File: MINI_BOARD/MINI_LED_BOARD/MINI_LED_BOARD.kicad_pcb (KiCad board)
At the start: 2 copper layers, 35 parts, among them J1 Conn_ARM_SWD_TagConnect_TC2030, J2 430450428, U1 MSPM0C1103SDDFR, U4 TPS76333DBVR

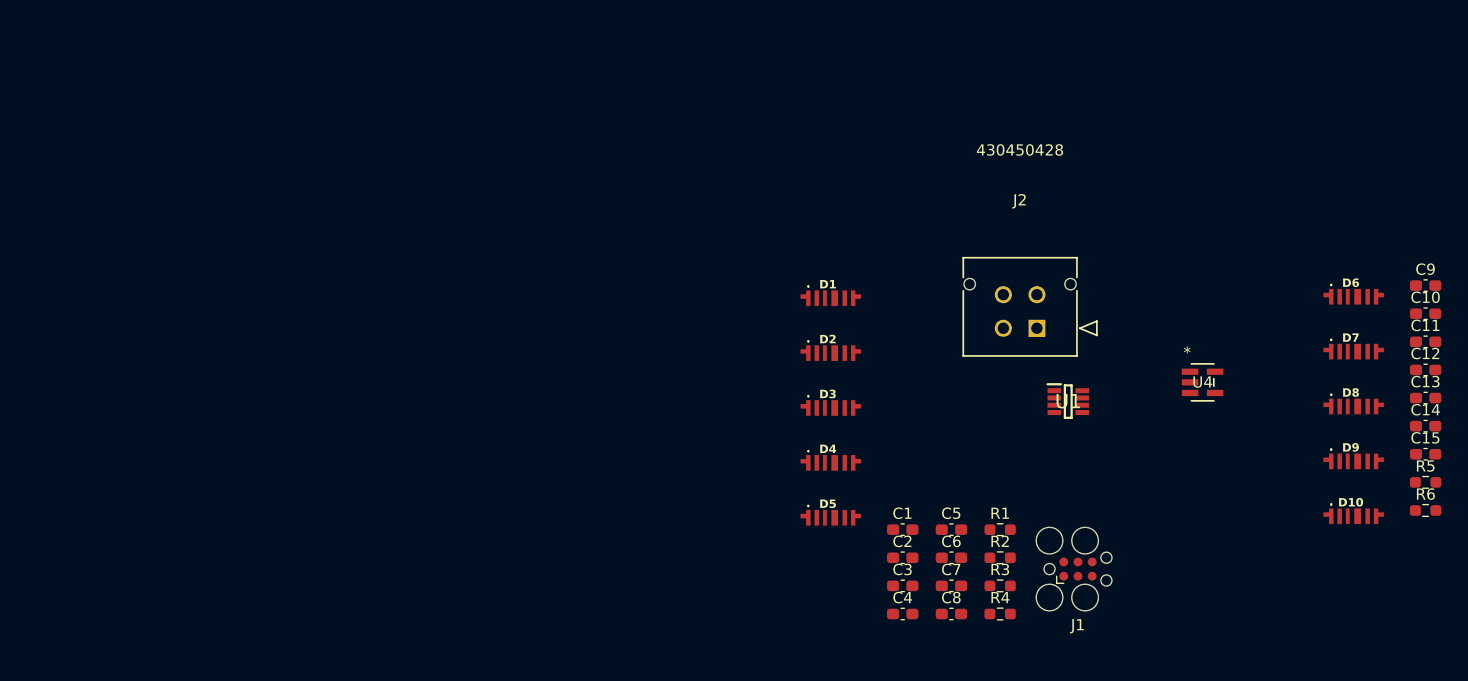
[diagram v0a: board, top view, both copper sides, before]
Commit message: Start laying out components
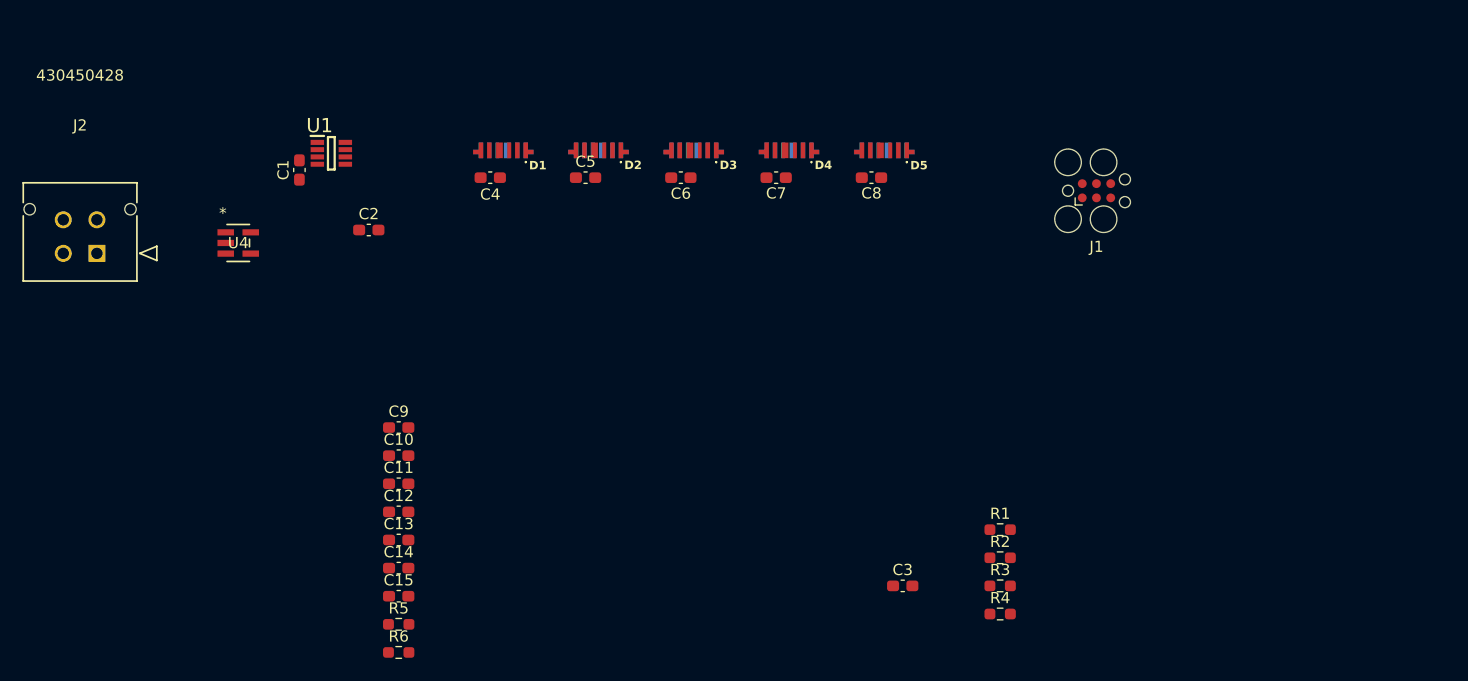
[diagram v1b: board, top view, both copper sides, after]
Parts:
- D10, D6, D7, D8, D9: moved to B.Cu
- moved C10 92.6 mm to (73.3, 82.5)
- moved C11 92.6 mm to (73.3, 85.0)
- moved C12 92.6 mm to (73.3, 87.5)
- moved C13 92.6 mm to (73.3, 90.0)
- moved C14 92.6 mm to (73.3, 92.5)
- moved C15 92.6 mm to (73.3, 95.1)
- moved C9 92.6 mm to (73.3, 80.0)
- moved R5 92.6 mm to (73.3, 97.6)
- moved R6 92.6 mm to (73.3, 100.1)
- moved U4 87.0 mm to (59.0, 63.5)
- moved J2 84.2 mm to (46.3, 64.4)
- moved D6 77.1 mm to (82.6, 54.9)
- moved D7 69.9 mm to (91.1, 54.9)
- moved U1 69.4 mm to (67.3, 55.5)
- moved D8 63.4 mm to (99.6, 54.9)
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
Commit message: Complete more major layout placement
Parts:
- C10, C11, C12, C13, C9: moved to B.Cu
- moved R1 66.2 mm to (70.6, 54.5)
- moved J1 63.0 mm to (73.0, 66.8)
- moved R3 62.4 mm to (78.2, 55.3), turned to 90 degrees
- moved C3 61.1 mm to (70.6, 55.9), turned to 180 degrees
- moved R2 59.5 mm to (78.1, 57.7), turned to 180 degrees
- moved C13 55.1 mm to (117.9, 57.7), turned to 180 degrees
- moved C12 46.8 mm to (109.4, 57.7), turned to 180 degrees
- moved R6 43.6 mm to (65.9, 57.1), turned to 180 degrees
- moved C15 40.1 mm to (65.9, 55.7)
- moved R5 39.7 mm to (65.9, 58.6)
- moved C14 39.2 mm to (59.7, 55.7), turned to -90 degrees
- moved C11 38.8 mm to (100.8, 57.7), turned to 180 degrees
- moved R4 36.8 mm to (123.6, 60.0)
- moved C10 31.3 mm to (92.3, 57.7), turned to 180 degrees
- moved C9 24.7 mm to (83.8, 57.7), turned to 180 degrees
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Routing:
- net Net-(U4-NC/FB): track 0.00 -> 4.41 mm
- net GND: track 0.00 -> 3.64 mm
- net +3.3V: track 0.00 -> 3.09 mm
- net +5V: track 0.00 -> 1.81 mm

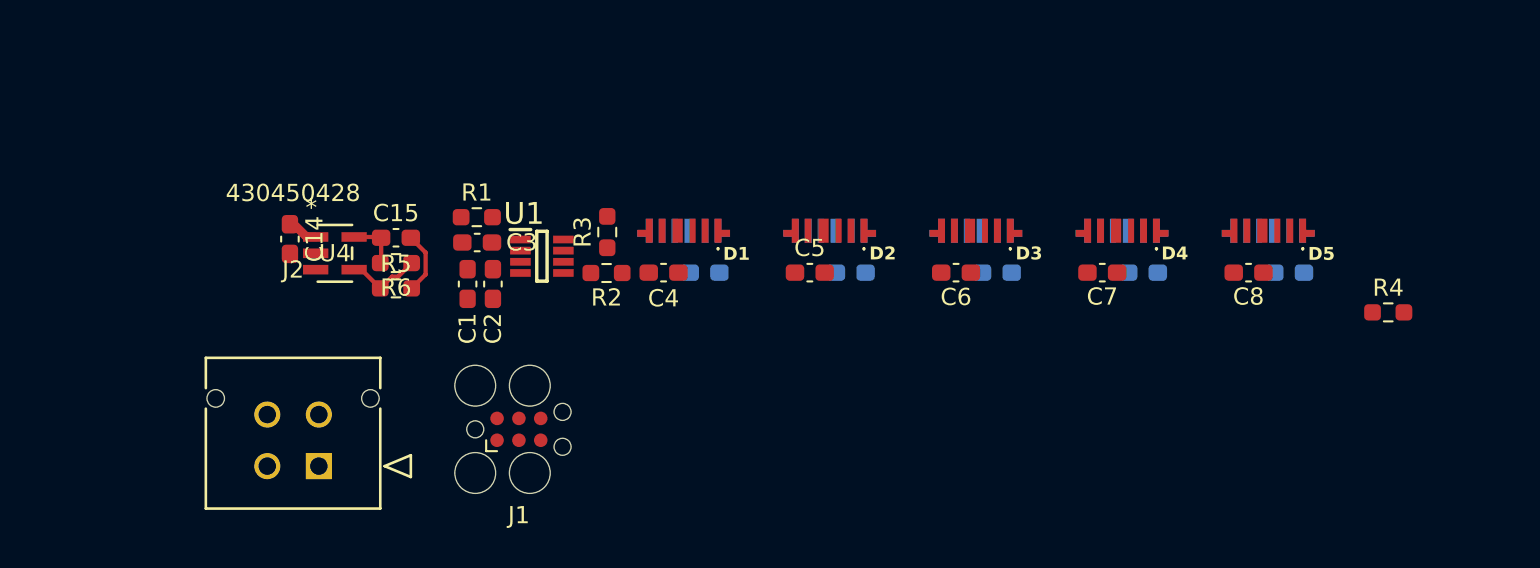
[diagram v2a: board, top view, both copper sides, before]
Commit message: Add more footprints and adjust layout placements
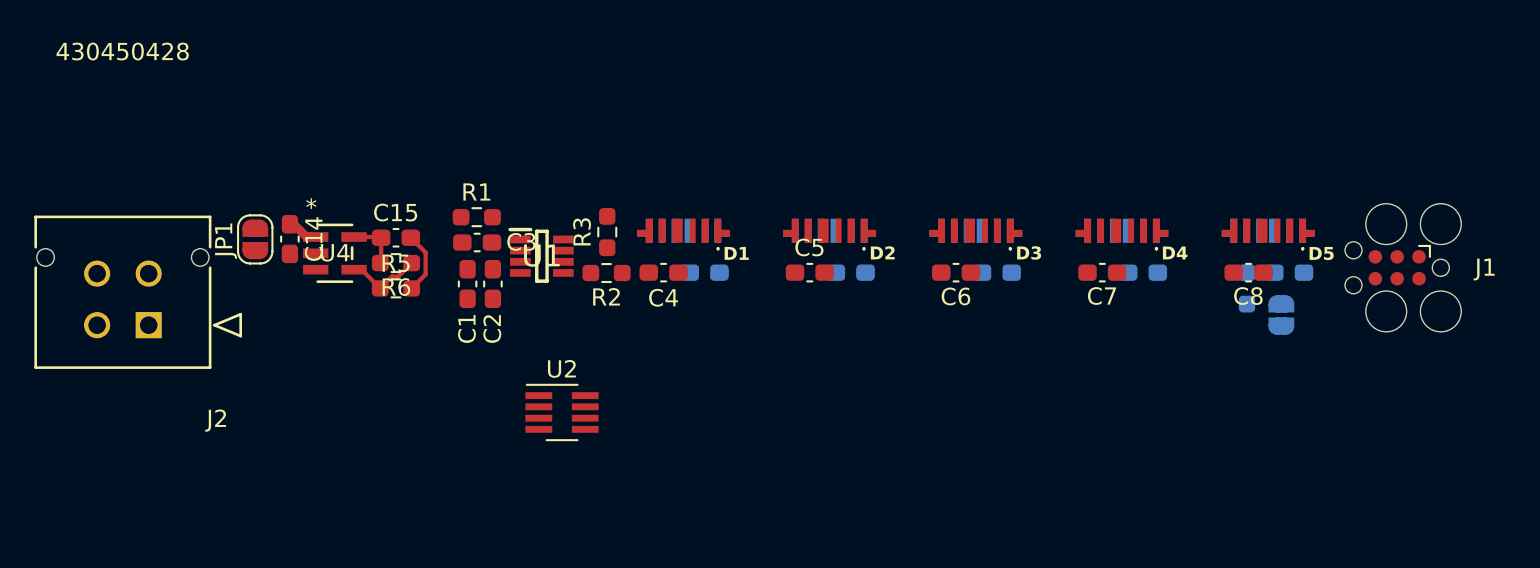
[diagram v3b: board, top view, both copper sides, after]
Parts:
- added JP1: SolderJumper_2_Open, Jumper:SolderJumper-2_P1.3mm_Open_RoundedPad1.0x1.5mm, F.Cu at (57.7, 55.7)
- added JP2: SolderJumper_2_Open, Jumper:SolderJumper-2_P1.3mm_Open_RoundedPad1.0x1.5mm, B.Cu at (117.4, 60.2)
- added U2: TCAN334, Package_TO_SOT_SMD:SOT-23-8_Handsoldering, F.Cu at (75.5, 65.8)
- R4: moved to B.Cu
- moved J1 52.0 mm to (124.1, 57.4), turned to 180 degrees
- moved J2 12.9 mm to (51.5, 60.7)
- moved R4 8.34 mm to (115.4, 58.6), turned to -90 degrees
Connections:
- R4 pad 2: unconnected-(R4-Pad2) -> Net-(JP2-A)

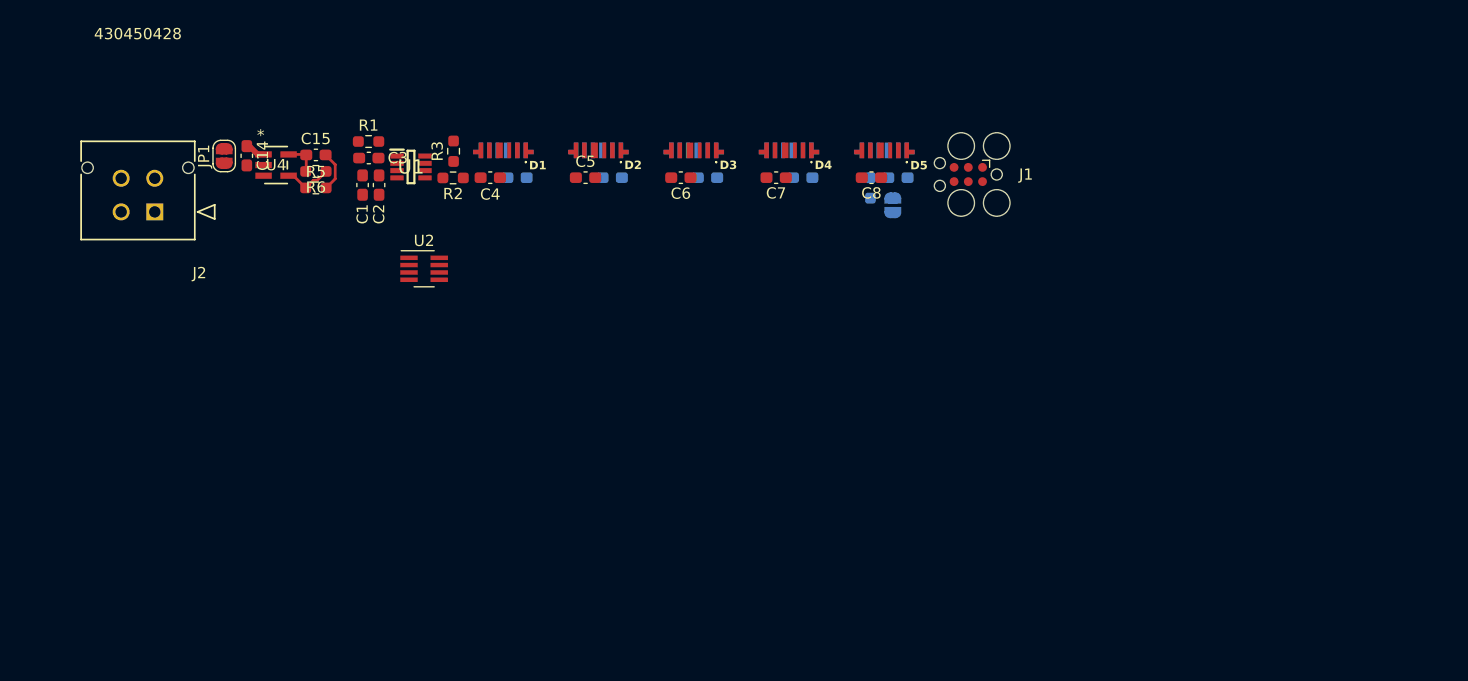
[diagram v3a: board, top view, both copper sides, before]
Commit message: Add more TCAN passives and mess with layout
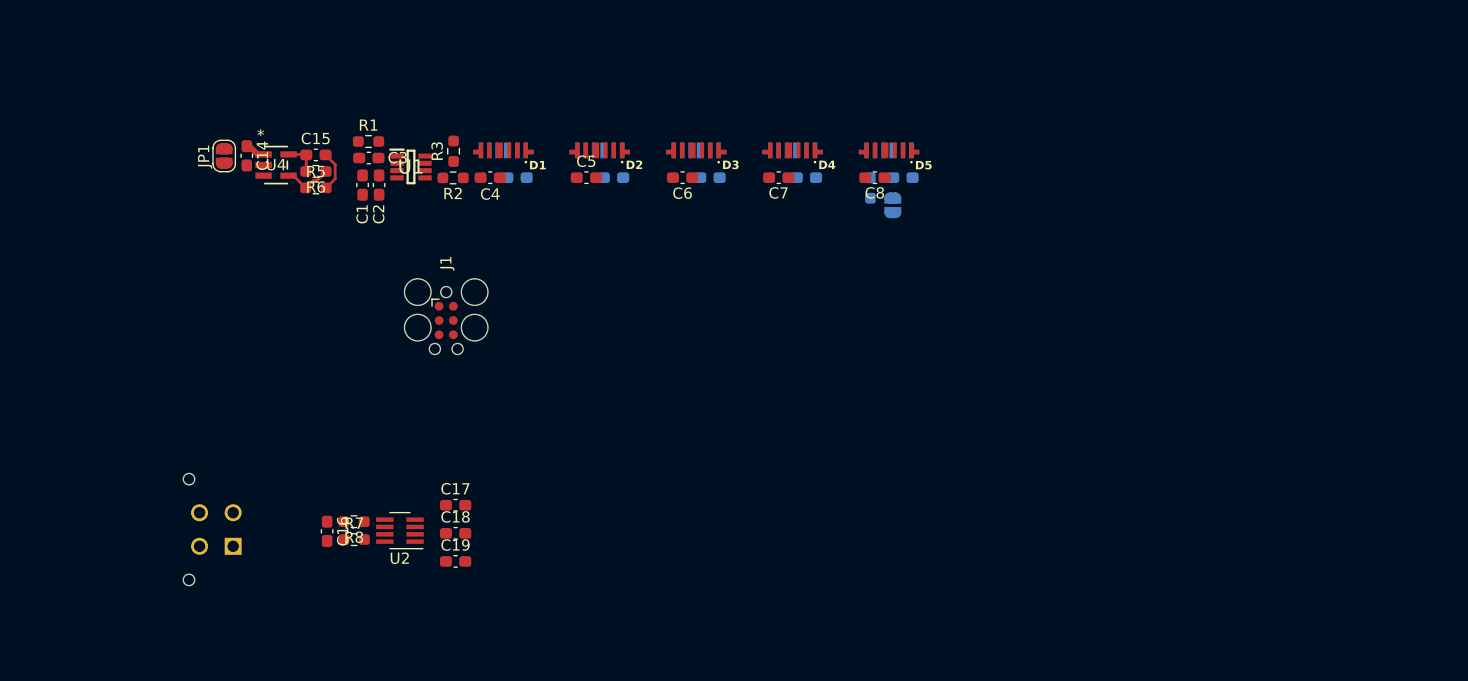
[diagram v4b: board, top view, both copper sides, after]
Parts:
- added C16: 1uF, Capacitor_SMD:C_0603_1608Metric_Pad1.08x0.95mm_HandSolder, F.Cu at (66.9, 89.3)
- added C17: 1uF, Capacitor_SMD:C_0603_1608Metric_Pad1.08x0.95mm_HandSolder, F.Cu at (78.4, 86.9)
- added C18: 1uF, Capacitor_SMD:C_0603_1608Metric_Pad1.08x0.95mm_HandSolder, F.Cu at (78.4, 89.4)
- added C19: 1uF, Capacitor_SMD:C_0603_1608Metric_Pad1.08x0.95mm_HandSolder, F.Cu at (78.4, 92.0)
- added R7: 60, Resistor_SMD:R_0603_1608Metric_Pad0.98x0.95mm_HandSolder, F.Cu at (69.3, 90.0)
- added R8: 60, Resistor_SMD:R_0603_1608Metric_Pad0.98x0.95mm_HandSolder, F.Cu at (69.3, 88.4)
- J2: moved to B.Cu
- moved J1 48.4 mm to (77.5, 70.4), turned to -90 degrees
- moved J2 30.7 mm to (58.5, 90.6), turned to -90 degrees
- moved U2 23.5 mm to (73.4, 89.2), turned to 180 degrees
- moved C13 0.45 mm to (118.3, 57.7)
- moved D10 0.43 mm to (117.1, 54.9)
- moved D5 0.42 mm to (117.1, 54.9)
- moved C12 0.33 mm to (109.7, 57.7)
- moved D9 0.33 mm to (108.5, 54.9)
- moved D4 0.32 mm to (108.5, 54.9)
- moved C8 0.31 mm to (115.8, 57.7)
- moved C7 0.23 mm to (107.2, 57.7)
- moved C11 0.22 mm to (101.1, 57.7)
- moved D8 0.22 mm to (99.8, 54.9)
- moved D3 0.21 mm to (99.8, 54.9)
- moved C6 0.15 mm to (98.6, 57.7)
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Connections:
- J2 pad 2: GND -> Net-(U2-CANH)
- J2 pad 3: Net-(U2-CANH) -> Net-(U2-CANL)
- J2 pad 4: Net-(U2-CANL) -> GND
- U2 pad 5: unconnected-(U2-SHDN-Pad5) -> Net-(U2-SHDN)
- U2 pad 8: unconnected-(U2-STB-Pad8) -> Net-(U2-STB)

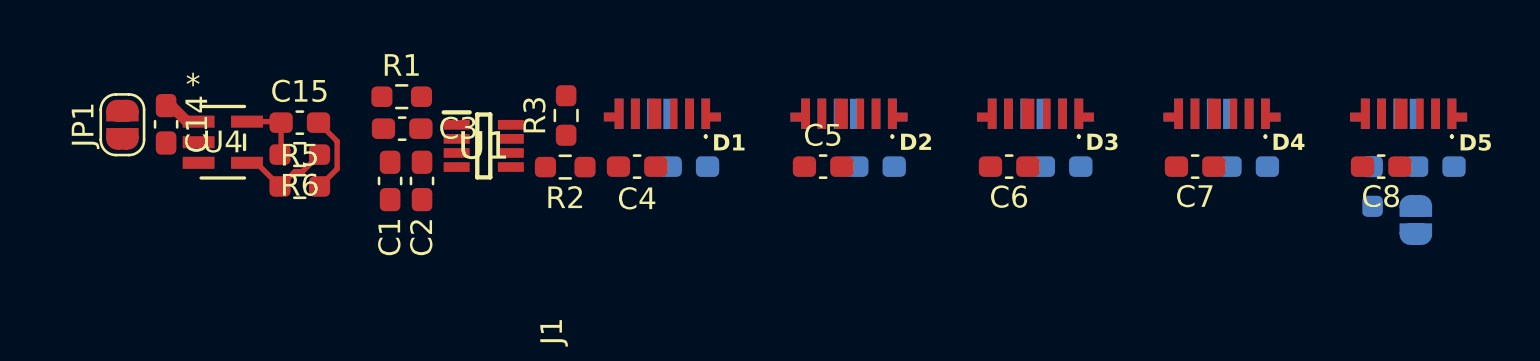
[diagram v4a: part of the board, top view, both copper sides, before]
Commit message: Create initial rough board edge
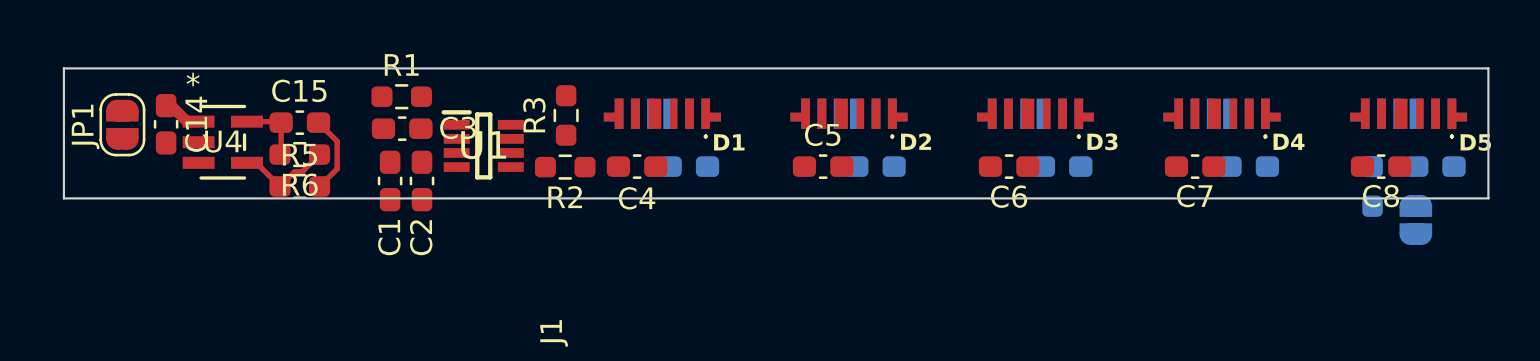
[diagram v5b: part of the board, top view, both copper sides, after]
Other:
- board outline added: 65.8 x 6 mm
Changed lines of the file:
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@@
     )
   )
-  (footprint "Connector:Tag-Connect_TC2030-IDC-FP_2x03_P1.27mm_Vertical" (layer "F.Cu")
+  (footprint "Connector:Tag-Connect_TC2030-IDC-FP_2x03_P1.27mm_Vertical" locked (layer "F.Cu")
     (at 77.525 70.44 -90)
     (descr "Tag-Connect programming header; http://www.tag-connect.com/Materials/TC2030-IDC.pdf")
@@
     (fp_line (start 3.75 4.25) (end -4.25 4.25)
       (stroke (width 0.05) (type solid)) (layer "F.CrtYd"))
-    (pad "" np_thru_hole circle (at -2.54 -2.54 270) (size 2.3749 2.3749) (drill 2.3749) (layers "*.Cu" "*.Mask"))
-    (pad "" np_thru_hole circle (at -2.54 0 270) (size 0.9906 0.9906) (drill 0.9906) (layers "*.Cu" "*.Mask"))
-    (pad "" np_thru_hole circle (at -2.54 2.54 270) (size 2.3749 2.3749) (drill 2.3749) (layers "*.Cu" "*.Mask"))
-    (pad "" np_thru_hole circle (at 0.635 -2.54 270) (size 2.3749 2.3749) (drill 2.3749) (layers "*.Cu" "*.Mask"))
-    (pad "" np_thru_hole circle (at 0.635 2.54 270) (size 2.3749 2.3749) (drill 2.3749) (layers "*.Cu" "*.Mask"))
-    (pad "" np_thru_hole circle (at 2.54 -1.016 270) (size 0.9906 0.9906) (drill 0.9906) (layers "*.Cu" "*.Mask"))
-    (pad "" np_thru_hole circle (at 2.54 1.016 270) (size 0.9906 0.9906) (drill 0.9906) (layers "*.Cu" "*.Mask"))
-    (pad "1" connect circle (at -1.27 0.635 270) (size 0.7874 0.7874) (layers "F.Cu" "F.Mask")
+    (pad "" np_thru_hole circle locked (at -2.54 -2.54 270) (size 2.3749 2.3749) (drill 2.3749) (layers "*.Cu" "*.Mask"))
+    (pad "" np_thru_hole circle locked (at -2.54 0 270) (size 0.9906 0.9906) (drill 0.9906) (layers "*.Cu" "*.Mask"))
+    (pad "" np_thru_hole circle locked (at -2.54 2.54 270) (size 2.3749 2.3749) (drill 2.3749) (layers "*.Cu" "*.Mask"))
+    (pad "" np_thru_hole circle locked (at 0.635 -2.54 270) (size 2.3749 2.3749) (drill 2.3749) (layers "*.Cu" "*.Mask"))
+    (pad "" np_thru_hole circle locked (at 0.635 2.54 270) (size 2.3749 2.3749) (drill 2.3749) (layers "*.Cu" "*.Mask"))
+    (pad "" np_thru_hole circle locked (at 2.54 -1.016 270) (size 0.9906 0.9906) (drill 0.9906) (layers "*.Cu" "*.Mask"))
+    (pad "" np_thru_hole circle locked (at 2.54 1.016 270) (size 0.9906 0.9906) (drill 0.9906) (layers "*.Cu" "*.Mask"))
+    (pad "1" connect circle locked (at -1.27 0.635 270) (size 0.7874 0.7874) (layers "F.Cu" "F.Mask")
       (net 1 "+3.3V") (pinfunction "VCC") (pintype "power_in"))
-    (pad "2" connect circle (at -1.27 -0.635 270) (size 0.7874 0.7874) (layers "F.Cu" "F.Mask")
+    (pad "2" connect circle locked (at -1.27 -0.635 270) (size 0.7874 0.7874) (layers "F.Cu" "F.Mask")
       (net 16 "Net-(J1-SWDIO)") (pinfunction "SWDIO") (pintype "bidirectional"))
-    (pad "3" connect circle (at 0 0.635 270) (size 0.7874 0.7874) (layers "F.Cu" "F.Mask")
+    (pad "3" connect circle locked (at 0 0.635 270) (size 0.7874 0.7874) (layers "F.Cu" "F.Mask")
       (net 3 "Net-(J1-~{RESET})") (pinfunction "~{RESET}") (pintype "open_collector"))
-    (pad "4" connect circle (at 0 -0.635 270) (size 0.7874 0.7874) (layers "F.Cu" "F.Mask")
+    (pad "4" connect circle locked (at 0 -0.635 270) (size 0.7874 0.7874) (layers "F.Cu" "F.Mask")
       (net 17 "Net-(J1-SWCLK)") (pinfunction "SWCLK") (pintype "output"))
-    (pad "5" connect circle (at 1.27 0.635 270) (size 0.7874 0.7874) (layers "F.Cu" "F.Mask")
+    (pad "5" connect circle locked (at 1.27 0.635 270) (size 0.7874 0.7874) (layers "F.Cu" "F.Mask")
       (net 2 "GND") (pinfunction "GND") (pintype "power_in"))
-    (pad "6" connect circle (at 1.27 -0.635 270) (size 0.7874 0.7874) (layers "F.Cu" "F.Mask")
+    (pad "6" connect circle locked (at 1.27 -0.635 270) (size 0.7874 0.7874) (layers "F.Cu" "F.Mask")
       (net 18 "unconnected-(J1-SWO-Pad6)") (pinfunction "SWO") (pintype "input+no_connect"))
     (zone (net 0) (net_name "") (layer "F.Cu") (hatch full 0.508)
@@
     )
   )
+  (gr_line (start 120.75 59.15) (end 120.75 53.15)
+    (stroke (width 0.1) (type default)) (layer "Edge.Cuts"))
+  (gr_line (start 55 53.15) (end 55 59.15)
+    (stroke (width 0.1) (type default)) (layer "Edge.Cuts"))
+  (gr_line (start 55 59.15) (end 120.75 59.15)
+    (stroke (width 0.1) (type default)) (layer "Edge.Cuts"))
+  (gr_line (start 120.75 53.15) (end 55 53.15)
+    (stroke (width 0.1) (type default)) (layer "Edge.Cuts"))
   (segment (start 64.979998 55.607798) (end 65.0258 55.6536) (width 0.25) (layer "F.Cu") (net 1))
   (segment (start 65.0258 55.6536) (end 65.0258 57.076) (width 0.25) (layer "F.Cu") (net 1))
